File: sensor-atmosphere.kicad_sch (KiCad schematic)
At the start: 1 part, among them U7 BME688

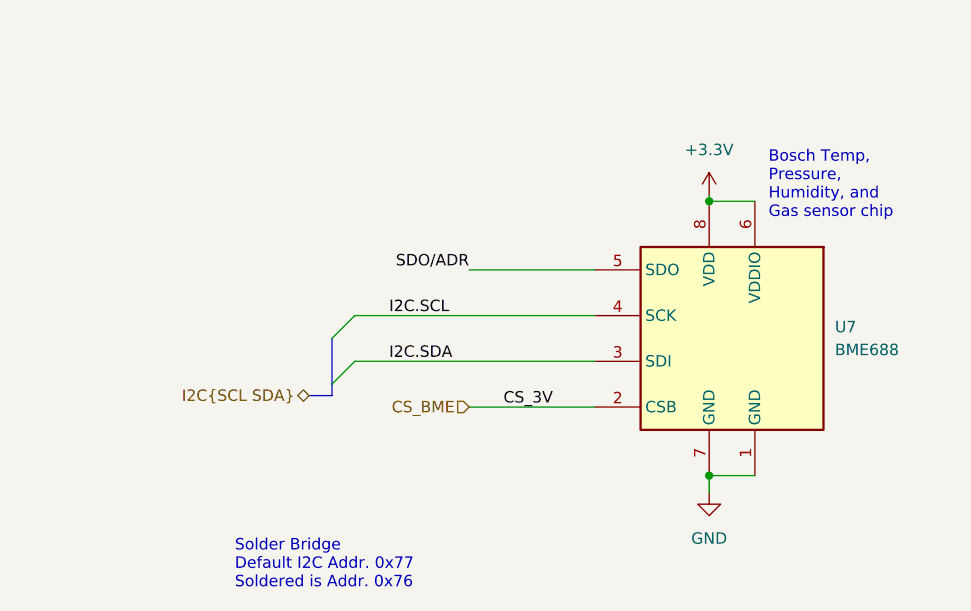
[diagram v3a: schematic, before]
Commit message: Spamming 0 ohm resistors
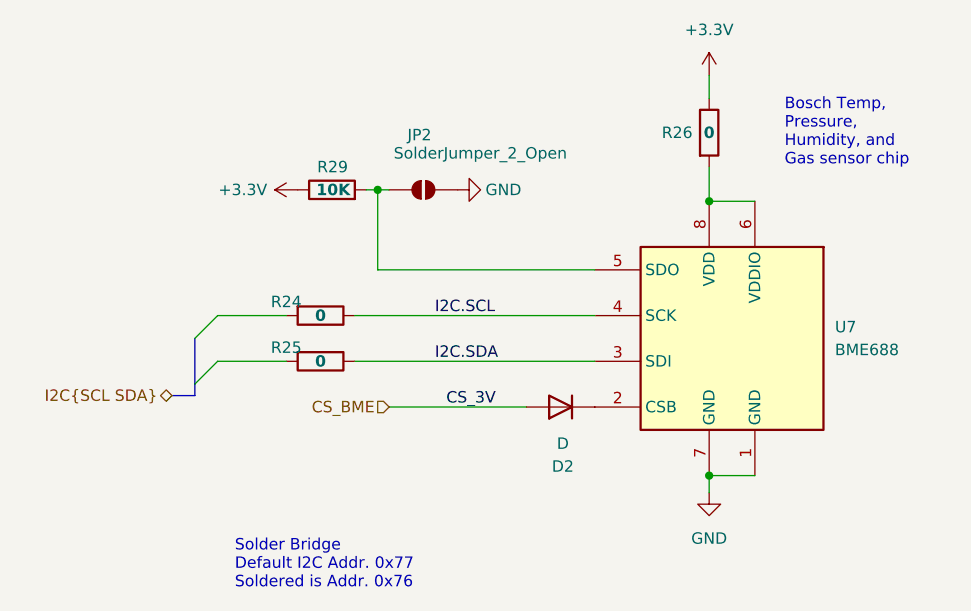
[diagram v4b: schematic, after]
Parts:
- added D2: D, symbol Device:D
- added JP2: SolderJumper_2_Open, Jumper:SolderJumper-2_P1.3mm_Open_TrianglePad1.0x1.5mm, symbol Jumper:SolderJumper_2_Open
- added R24, R25, R26: 0, Resistor_SMD:R_0603_1608Metric, symbol Device:R
- added R29: 10K, Resistor_SMD:R_0603_1608Metric, symbol Device:R
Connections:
- net +3.3V: now also R26.1, R29.1; no longer U7.6 (VDDIO), U7.8 (VDD)
- net CS_BME: now also D2.2 (A); no longer U7.2 (CSB)
- net GND: now also JP2.1 (A)
- net I2C.SCL: now also R24.1
- net I2C.SDA: now also R25.1
- net SDO/ADR: no longer names the net of U7.5 (SDO)
- net SDO/ADR: now also JP2.2 (B), R29.2
- new net: D2.1 (K), U7.2 (CSB)
- new net: R26.2, U7.6 (VDDIO), U7.8 (VDD)
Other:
- title: (none) -> Sensor - Atmosphere

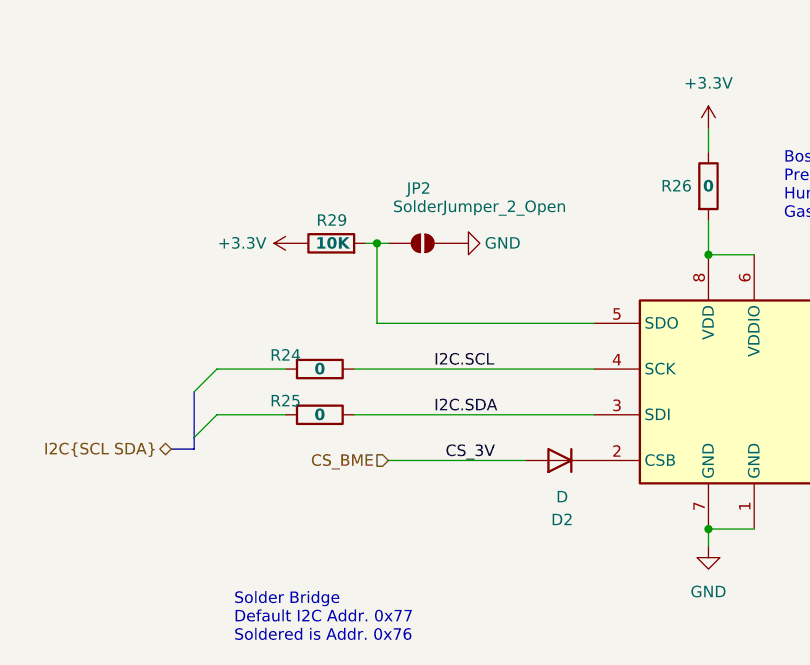
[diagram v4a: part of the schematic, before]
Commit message: Adding more 0 ohm resistors and pullups for I2C lines
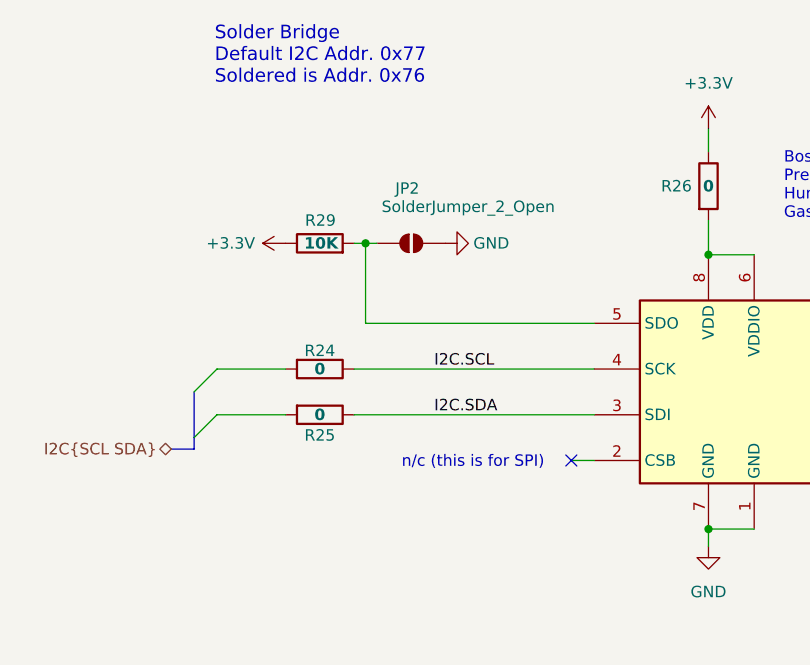
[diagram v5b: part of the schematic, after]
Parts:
- removed D2: D, symbol Device:D
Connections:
- no-connect marks 0 -> 1
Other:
- note added: "n/c (this is for SPI)"
- moved on the sheet: JP2, R29

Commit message: Fixing lots of ERC errors
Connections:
- net I2C.SCL: now also R24.2; no longer R24.1, U7.4 (SCK)
- net I2C.SDA: now also R25.2; no longer R25.1, U7.3 (SDI)
- net +3.3V renamed +3V3
- new net: R24.1, U7.4 (SCK)
- new net: R25.1, U7.3 (SDI)
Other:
- moved on the sheet: JP2, R24, R25, R26, R29

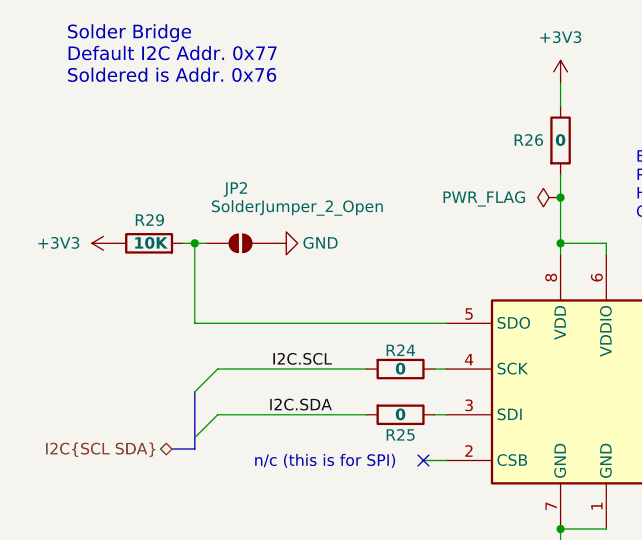
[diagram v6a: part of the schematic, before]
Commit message: Added mounting holes
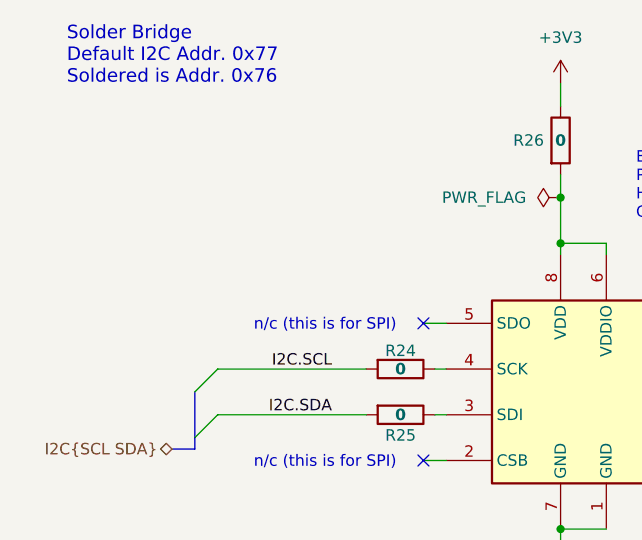
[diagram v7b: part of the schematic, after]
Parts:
- removed JP2: SolderJumper_2_Open, Jumper:SolderJumper-2_P1.3mm_Open_TrianglePad1.0x1.5mm, symbol Jumper:SolderJumper_2_Open
- removed R29: 10K, Resistor_SMD:R_0603_1608Metric, symbol Device:R
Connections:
- no-connect marks 1 -> 2

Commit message: Creating fab package
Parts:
- R24, R25, R26: Supplier_1 Price @ Qty $0.00304 -> 0.00304; Supplier_1 Unit Price $0.10000 -> 0.10000
- U7: Supplier_1 Price @ Qty (none) -> 5.94891; Supplier_1 Unit Price (none) -> 12.35000
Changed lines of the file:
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@@
 			)
 		)
-		(property "Supplier_1 Unit Price" "$0.10000 "
+		(property "Supplier_1 Unit Price" "0.10000 "
 			(at 144.78 77.47 0)
 			(effects
@@
 			)
 		)
-		(property "Supplier_1 Price @ Qty" "$0.00304 "
+		(property "Supplier_1 Price @ Qty" "0.00304 "
 			(at 144.78 77.47 0)
 			(effects
@@
 			)
 		)
-		(property "Supplier_1 Unit Price" "$0.10000 "
-			(at 144.78 82.55 0)
-			(effects
-				(font
-					(size 1.27 1.27)
-				)
-				(hide yes)
-			)
-		)
-		(property "Supplier_1 Price @ Qty" "$0.00304 "
+		(property "Supplier_1 Unit Price" "0.10000 "
+			(at 144.78 82.55 0)
+			(effects
+				(font
+					(size 1.27 1.27)
+				)
+				(hide yes)
+			)
+		)
+		(property "Supplier_1 Price @ Qty" "0.00304 "
 			(at 144.78 82.55 0)
 			(effects
@@
 			)
 		)
+		(property "Supplier_1" ""
+			(at 165.1 80.01 0)
+			(effects
+				(font
+					(size 1.27 1.27)
+				)
+				(hide yes)
+			)
+		)
+		(property "Supplier_1 P/N" ""
+			(at 165.1 80.01 0)
+			(effects
+				(font
+					(size 1.27 1.27)
+				)
+				(hide yes)
+			)
+		)
+		(property "Supplier_1 Unit Price" "12.35000"
+			(at 165.1 80.01 0)
+			(effects
+				(font
+					(size 1.27 1.27)
+				)
+				(hide yes)
+			)
+		)
+		(property "Supplier_1 Price @ Qty" "5.94891"
+			(at 165.1 80.01 0)
+			(effects
+				(font
+					(size 1.27 1.27)
+				)
+				(hide yes)
+			)
+		)
+		(property "Supplier_2" ""
+			(at 165.1 80.01 0)
+			(effects
+				(font
+					(size 1.27 1.27)
+				)
+				(hide yes)
+			)
+		)
+		(property "Supplier_2 P/N" ""
+			(at 165.1 80.01 0)
+			(effects
+				(font
+					(size 1.27 1.27)
+				)
+				(hide yes)
+			)
+		)
+		(property "Supplier_2 Unit Price" ""
+			(at 165.1 80.01 0)
+			(effects
+				(font
+					(size 1.27 1.27)
+				)
+				(hide yes)
+			)
+		)
+		(property "Field21" ""
+			(at 165.1 80.01 0)
+			(effects
+				(font
+					(size 1.27 1.27)
+				)
+				(hide yes)
+			)
+		)
+		(property "Supplier_2 Price @ Qty" ""
+			(at 165.1 80.01 0)
+			(effects
+				(font
+					(size 1.27 1.27)
+				)
+				(hide yes)
+			)
+		)
 		(pin "1"
 		)
@@
 			)
 		)
-		(property "Supplier_1 Unit Price" "$0.10000 "
-			(at 162.56 52.07 0)
-			(effects
-				(font
-					(size 1.27 1.27)
-				)
-				(hide yes)
-			)
-		)
-		(property "Supplier_1 Price @ Qty" "$0.00304 "
-			(at 162.56 52.07 0)
-			(effects
+		(property "Supplier_1 Unit Price" "0.10000 "
+			(at 162.56 52.07 0)
+			(effects
+				(font
+					(size 1.27 1.27)
+				)
+				(hide yes)
+			)
+		)
+		(property "Supplier_1 Price @ Qty" "0.00304 "
+			(at 162.56 52.07 0)
+			(effects
